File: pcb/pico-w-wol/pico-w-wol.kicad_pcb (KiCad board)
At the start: 2 copper layers, 8 x 26.2 mm, 4 parts, among them J1 pc button input (passthrough 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, J2 pc output, U1 PC817, U2 Pico

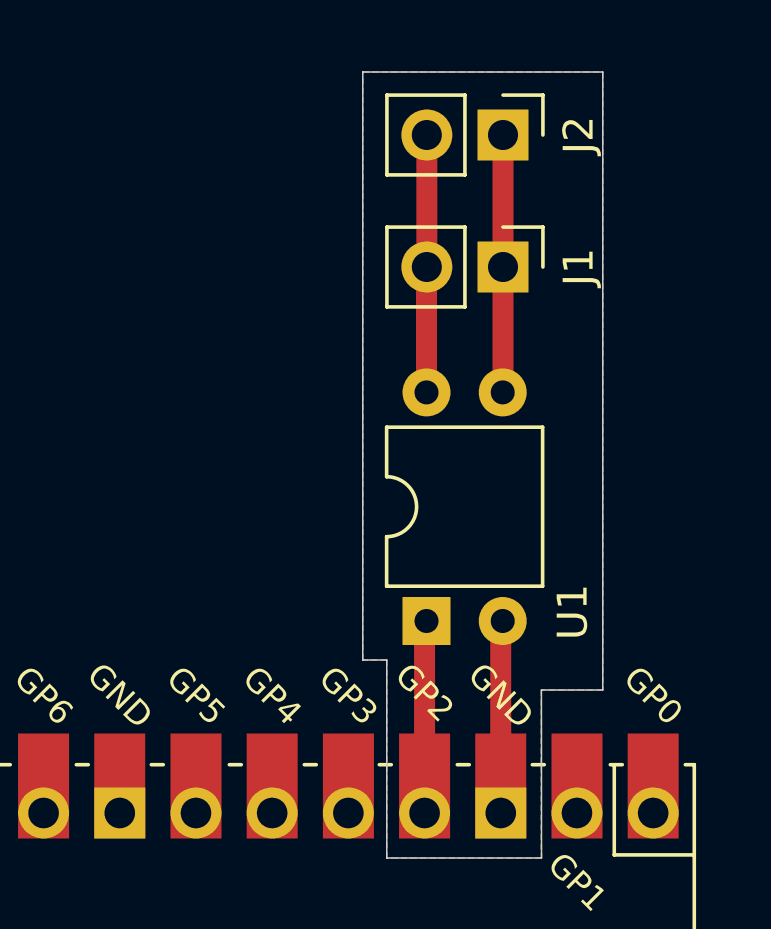
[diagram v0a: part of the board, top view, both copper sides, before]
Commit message: Updated pcb labeling
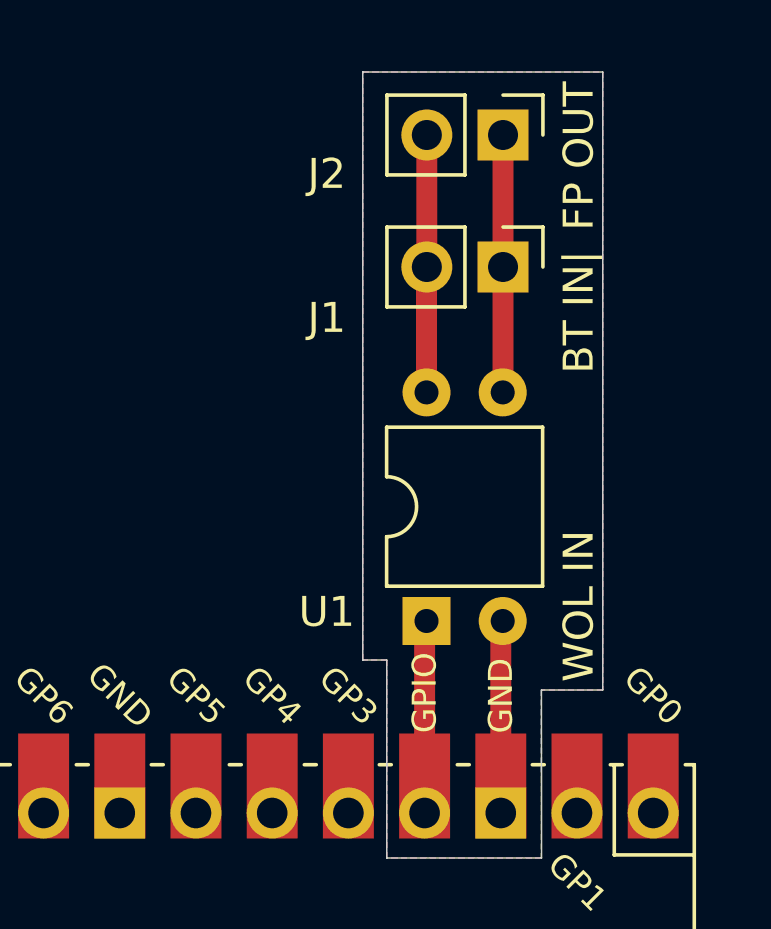
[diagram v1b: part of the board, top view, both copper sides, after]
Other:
- board text added: "BT IN|"
- board text added: "FP OUT"
- board text added: "WOL IN"
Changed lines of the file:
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@@
 		)
 		(fp_text user "GND"
-			(at -12.8 -19.05 135)
+			(at -12.8 -19.05 90)
 			(layer "F.SilkS")
 			(effects
@@
 			)
 		)
-		(fp_text user "GP2"
-			(at -12.9 -16.51 135)
+		(fp_text user "GPIO"
+			(at -12.9 -16.51 90)
 			(layer "F.SilkS")
 			(effects
@@
 				(font
 					(size 0.8 0.8)
-					(thickness 0.15)
-				)
-			)
-		)
-		(fp_text user "Copper Keepouts shown on Dwgs layer"
-			(at 0.1 -30.2 90)
-			(layer "Cmts.User")
-			(effects
-				(font
-					(size 1 1)
 					(thickness 0.15)
 				)
@@
 		(tags "THT DIP DIL PDIP 2.54mm 7.62mm 300mil")
 		(property "Reference" "U1"
-			(at 0.3 4.875 90)
+			(at 0.3 -3.325 180)
 			(layer "F.SilkS")
 			(effects
@@
 		)
 		(property "Value" "PC817"
-			(at 3.81 4.87 90)
+			(at 1.7 -4.925 180)
 			(layer "F.Fab")
 			(effects
@@
 		(tags "Through hole pin header THT 1x02 2.54mm single row")
 		(property "Reference" "J1"
-			(at 0 -2.525 90)
+			(at 1.7 5.875 180)
 			(layer "F.SilkS")
 			(effects
@@
 		)
 		(property "Value" "pc button input (passthrough port)"
-			(at 8.7 6.475 90)
+			(at -0.1 18.275 180)
 			(layer "F.Fab")
 			(effects
@@
 		(tags "Through hole pin header THT 1x02 2.54mm single row")
 		(property "Reference" "J2"
-			(at 0 -2.525 90)
+			(at 1.3 5.875 180)
 			(layer "F.SilkS")
 			(effects
@@
 		)
 		(property "Value" "pc output"
-			(at -4.3 6.675 90)
+			(at -0.3 8.475 180)
 			(layer "F.Fab")
 			(effects
@@
 		(layer "Edge.Cuts")
 	)
+	(gr_text "WOL IN"
+		(at 118.8 105.8 90)
+		(layer "F.SilkS")
+		(effects
+			(font
+				(size 1 1)
+				(thickness 0.15)
+			)
+		)
+	)
+	(gr_text "FP OUT"
+		(at 118.8 90.8 90)
+		(layer "F.SilkS")
+		(effects
+			(font
+				(size 1 1)
+				(thickness 0.15)
+			)
+		)
+	)
+	(gr_text "BT IN|"
+		(at 118.8 96 90)
+		(layer "F.SilkS")
+		(effects
+			(font
+				(size 1 1)
+				(thickness 0.15)
+			)
+		)
+	)
 	(segment

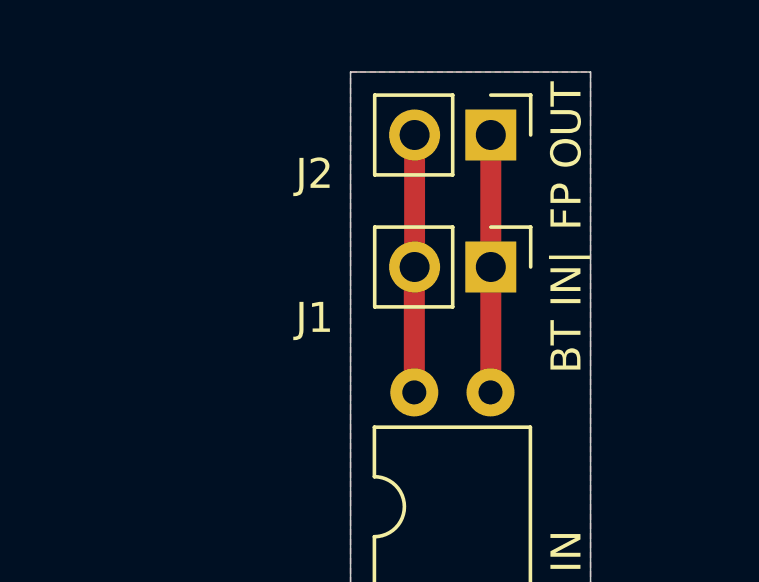
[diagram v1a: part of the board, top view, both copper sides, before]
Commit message: Updated silkscreen
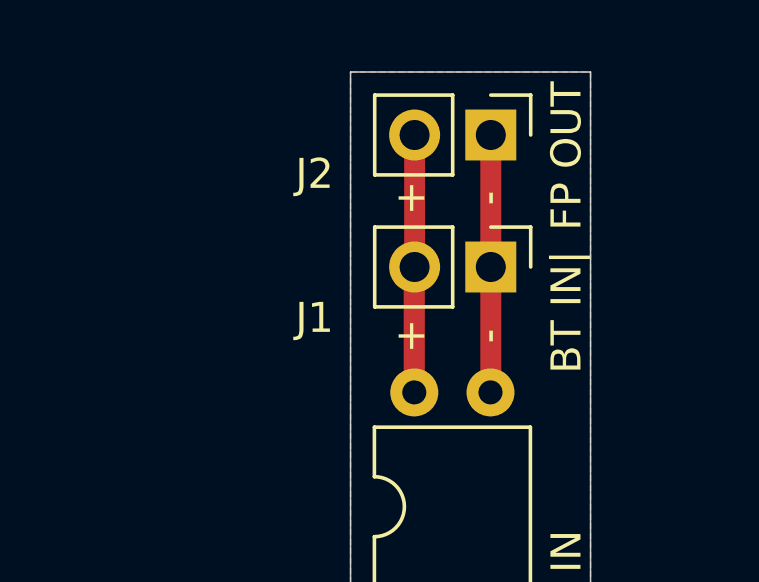
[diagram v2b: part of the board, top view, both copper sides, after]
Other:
- board text added: "+"
- board text added: "-"
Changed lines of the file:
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@@
 		(layer "Edge.Cuts")
+	)
+	(gr_text "-"
+		(at 116.2 96.8 90)
+		(layer "F.SilkS")
+		(effects
+			(font
+				(size 1 1)
+				(thickness 0.15)
+			)
+		)
+	)
+	(gr_text "+"
+		(at 113.6 92.2 90)
+		(layer "F.SilkS")
+		(effects
+			(font
+				(size 1 1)
+				(thickness 0.15)
+			)
+		)
 	)
 	(gr_text "WOL IN"
@@
 		(layer "F.SilkS")
 		(effects
+			(font
+				(size 1 1)
+				(thickness 0.15)
+			)
+		)
+	)
+	(gr_text "+"
+		(at 113.6 96.8 90)
+		(layer "F.SilkS")
+		(effects
+			(font
+				(size 1 1)
+				(thickness 0.15)
+			)
+		)
+	)
+	(gr_text "-"
+		(at 116.2 92.2 90)
+		(layer "F.SilkS")
+		(effects
